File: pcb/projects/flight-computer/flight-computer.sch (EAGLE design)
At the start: 83 parts, among them IC1 ADG609RU, IC3 ADG609RU, P1 53048-0810, P2 53048-0810, U1 MCP73831/OT, U12 MAX31856MUD+, U13 MAX31856MUD+, U2 LP2985IM5-1.8/NOPB, U3 COM-13909, U4 ADXL377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

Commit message: add activation redundancy processor
- partial update of documentation to reflect this addition
- extra diagram of redundant activation
- pcb update to include a 32 pin qfn samd21 cortex m0 processor and necessary connections to bootload and flash over USB
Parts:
- removed ISM_SW: (no value), adafruit:PINHD-1X3CB
- added C7: 1uF, microbuilder:CAP_CERAMIC0603_NO
- added CN1: 4U#20329, microbuilder:USB_MICRO_20329_V2
- added IC2: ATSAMD21E, microbuilder:ATSAMD21E
- added JP1: (no value), pinhead:PINHD-1X4
- added JP2: (no value), pinhead:PINHD-1X2
- added R17: 470, rcl:R-US_R0603
- added SJ1: (no value), jumper:SJ
- added U10: SN74LVC1G08DCKR, SN74LVC1G08DCKR:SN74LVC1G08DCKR
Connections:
- removed net RADIO_OFF_SIG: ISM_SW.1, R18.1, U$1.33/A14
- new net !RESET: IC2./RESET, JP1.3
- new net D+: CN1.D+, IC2.PA25/I13/SERCOM3+5.3/D+
- new net D-: CN1.D-, IC2.PA24/I12/SERCOM3+5.2/D-
- new net PRI_ACT: SJ1.1, U$1.23/A9, U10.A
- new net SEC_ACT: IC2.PA00/EINT0/SERCOM1.0, SJ1.2, U10.B
- new net SEC_CS: IC2.PA08/I2C/AIN16/SERCOM0+2.0/I2SD1, U$1.27
- new net SEC_EN: IC2.PA01/EINT1/SERCOM1.1, R17.1, U$1.39/A20
- new net SWCLK: IC2.PA30/I10/SECOM1.2/SWCLK, JP1.2
- new net SWDIO: IC2.PA31/I11/SECOM1.3/SWDIO, JP1.1
- new net VBUS: CN1.VBUS
- new net VDDCORE1: C7.1, IC2.VDDCORE
- net 3V3: now also IC2.VDDA, IC2.VDDIN, JP2.1, U10.VCC; no longer ISM_SW.2
- net 3V3_RADIO: now also JP2.2, R18.1, U$1.33/A14; no longer ISM_SW.3
- net ACT: now also U10.Y; no longer U$1.23/A9
- net CS@TC1: now also IC2.PA02/EINT2/AIN0/Y0/VOUT
- net CS@TC2: now also IC2.PA10/I10/AIN18/SERCOM0+2.2/I2SCK
- net GND: now also C7.2, CN1.GND, IC2.GND, IC2.GNDA, JP1.4, R17.2, U10.GND
- net MISO: now also IC2.PA09/I2C/I9/AIN17/SERCOM0+2.1/I2SMC
- net MOSI: now also IC2.PA06/EINT6/AIN6/SERCOM0.2
- net SCLK: now also IC2.PA07/I7/AIN7/SERCOM0.3/I2SD0
- net TC1_FAULT: now also IC2.PA14/I14/SERCOM2+4.2
- net TC2_FAULT: now also IC2.PA15/I15/SERCOM3+4.3
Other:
- note added: "Secondary TC Monitoring System"
- note added: "Thanks to the design files and hard work done by Adafruit for the Trinket M0"
- note added: "https://cdn-learn.adafruit.com/assets/assets/000/049/778/original/adafruit_products_Adafruit_Trinket_M0.png?1514756138 https://github.com/adafruit/Adafruit-Trinket-M0-PCB"

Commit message: updated documentation, BOM and pinmap for activation redundancy processor
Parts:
- added JP3: (no value), pinhead:PINHD-1X2
- added R19: 100, rcl:R-US_R0603
- R17: value 470 -> 10k
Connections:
- new net BUZZER: JP3.1, U$1.24
- new net N$2: JP3.2, R19.2
- net GND: now also R19.1
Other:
- note added: "Activation Redundancy Processor"
- note added: "Buzzer Header"
- note removed: "Secondary TC Monitoring System"
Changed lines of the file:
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@@
 <part name="U$5" library="microbuilder" deviceset="VBUS" device=""/>
 <part name="SJ1" library="jumper" library_urn="urn:adsk.eagle:library:252" deviceset="SJ" device="" package3d_urn="urn:adsk.eagle:package:15471/1"/>
-<part name="R17" library="rcl" library_urn="urn:adsk.eagle:library:334" deviceset="R-US_" device="R0603" package3d_urn="urn:adsk.eagle:package:23555/3" value="470"/>
+<part name="R17" library="rcl" library_urn="urn:adsk.eagle:library:334" deviceset="R-US_" device="R0603" package3d_urn="urn:adsk.eagle:package:23555/3" value="10k"/>
+<part name="JP3" library="pinhead" deviceset="PINHD-1X2" device="" package3d_urn="urn:adsk.eagle:package:22435/2"/>
+<part name="R19" library="rcl" library_urn="urn:adsk.eagle:library:334" deviceset="R-US_" device="R0603" package3d_urn="urn:adsk.eagle:package:23555/3" value="100"/>
 </parts>
 <sheets>
@@
 <wire x1="63.5" y1="27.94" x2="71.12" y2="27.94" width="0.1524" layer="91"/>
 <label x="63.5" y="27.94" size="1.778" layer="95"/>
+</segment>
+</net>
+<net name="BUZZER" class="0">
+<segment>
+<pinref part="U$1" gate="G$1" pin="24"/>
+<wire x1="22.86" y1="33.02" x2="17.78" y2="33.02" width="0.1524" layer="91"/>
+<label x="10.16" y="33.02" size="1.778" layer="95"/>
 </segment>
 </net>
@@
 <sheet>
 <plain>
-<wire x1="147.32" y1="35.56" x2="147.32" y2="96.52" width="0.254" layer="94" style="longdash"/>
+<wire x1="147.32" y1="35.56" x2="147.32" y2="45.72" width="0.254" layer="94" style="longdash"/>
+<wire x1="147.32" y1="45.72" x2="147.32" y2="96.52" width="0.254" layer="94" style="longdash"/>
 <wire x1="147.32" y1="96.52" x2="147.32" y2="175.26" width="0.254" layer="94" style="longdash"/>
 <wire x1="147.32" y1="175.26" x2="147.32" y2="185.42" width="0.254" layer="94" style="longdash"/>
@@
 <wire x1="147.32" y1="96.52" x2="0" y2="96.52" width="0.254" layer="94" style="longdash"/>
 <text x="38.1" y="88.9" size="5.08" layer="94">Capacitive Sense Header</text>
+<wire x1="147.32" y1="45.72" x2="0" y2="45.72" width="0.254" layer="94" style="longdash"/>
+<text x="38.1" y="38.1" size="5.08" layer="94">Buzzer Header</text>
 </plain>
 <instances>
@@
 <instance part="GND6" gate="1" x="35.56" y="55.88" smashed="yes">
 <attribute name="VALUE" x="33.02" y="53.34" size="1.778" layer="96"/>
+</instance>
+<instance part="JP3" gate="G$1" x="66.04" y="22.86" smashed="yes">
+<attribute name="NAME" x="59.69" y="28.575" size="1.778" layer="95"/>
+<attribute name="VALUE" x="59.69" y="17.78" size="1.778" layer="96"/>
+</instance>
+<instance part="R19" gate="G$1" x="48.26" y="22.86" smashed="yes">
+<attribute name="NAME" x="44.45" y="24.3586" size="1.778" layer="95"/>
+<attribute name="VALUE" x="44.45" y="19.558" size="1.778" layer="96"/>
 </instance>
 </instances>
@@
 <wire x1="104.14" y1="157.48" x2="104.14" y2="109.22" width="0.1524" layer="91"/>
 </segment>
+<segment>
+<pinref part="R19" gate="G$1" pin="1"/>
+<wire x1="43.18" y1="22.86" x2="35.56" y2="22.86" width="0.1524" layer="91"/>
+<wire x1="35.56" y1="22.86" x2="35.56" y2="15.24" width="0.1524" layer="91"/>
+<label x="35.56" y="15.24" size="1.778" layer="95"/>
+</segment>
 </net>
 <net name="MISO" class="0">
@@
 </segment>
 </net>
+<net name="N$2" class="0">
+<segment>
+<pinref part="JP3" gate="G$1" pin="2"/>
+<pinref part="R19" gate="G$1" pin="2"/>
+<wire x1="63.5" y1="22.86" x2="53.34" y2="22.86" width="0.1524" layer="91"/>
+</segment>
+</net>
+<net name="BUZZER" class="0">
+<segment>
+<pinref part="JP3" gate="G$1" pin="1"/>
+<wire x1="63.5" y1="25.4" x2="35.56" y2="25.4" width="0.1524" layer="91"/>
+<label x="35.56" y="25.4" size="1.778" layer="95"/>
+</segment>
+</net>
 </nets>
 </sheet>
 <sheet>
 <plain>
-<text x="30.48" y="195.58" size="10.16" layer="94">Secondary TC Monitoring System</text>
+<text x="30.48" y="195.58" size="7.62" layer="94">Activation Redundancy Processor</text>
 <text x="119.38" y="149.86" size="2.032" layer="94">Thanks to the design files and hard work done by Adafruit for the Trinket M0</text>
 <text x="119.38" y="137.16" size="2.032" layer="94">https://cdn-learn.adafruit.com/assets/assets/000/049/778/original/adafruit_products_Adafruit_Trinket_M0.png?1514756138

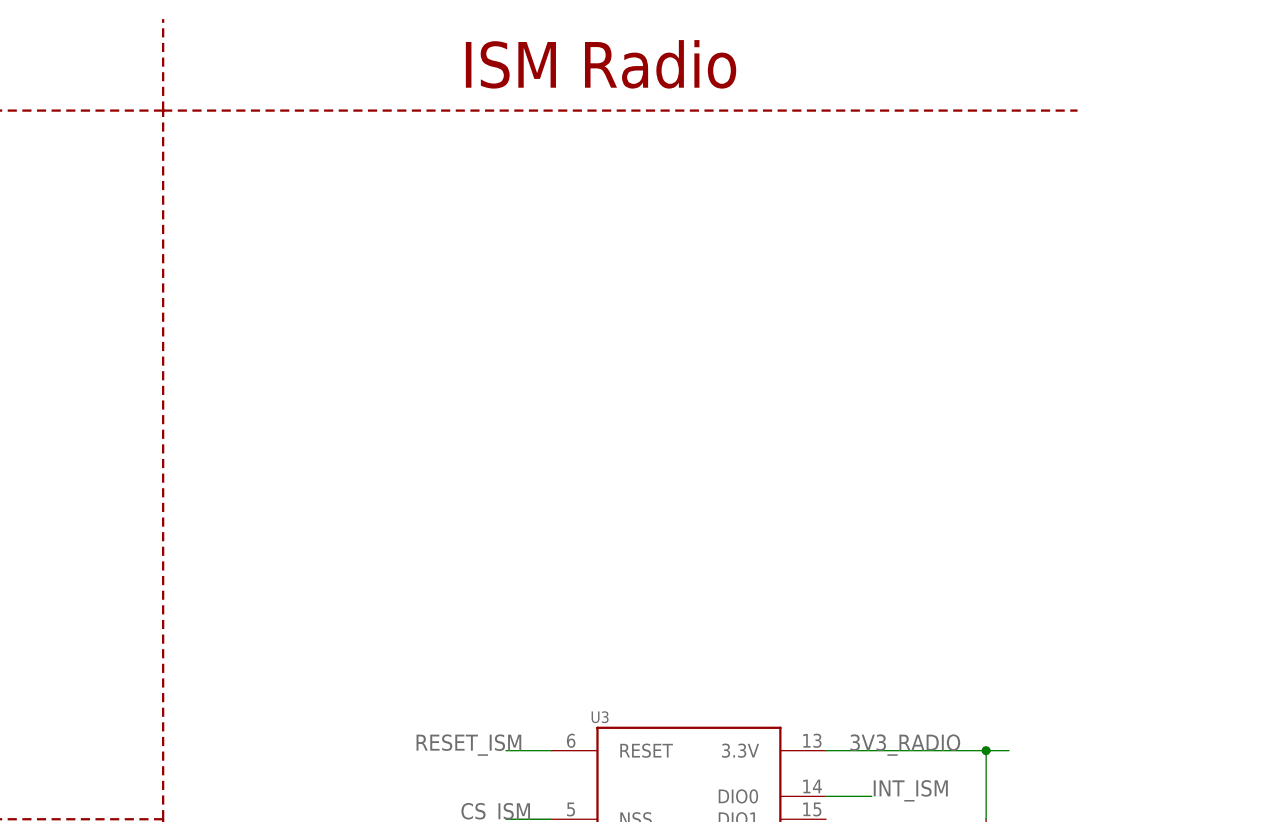
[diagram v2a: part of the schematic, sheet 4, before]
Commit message: add v1.1 pcb and documentation - added DSP310 barometric pressure sensor - add buzzer - add capacitive sense header - add more interface pins to the safety processor - add arduino pinouts for safety processor and refs on board silk - update flight computer hardware manual - add gerbers for v1.1 boards
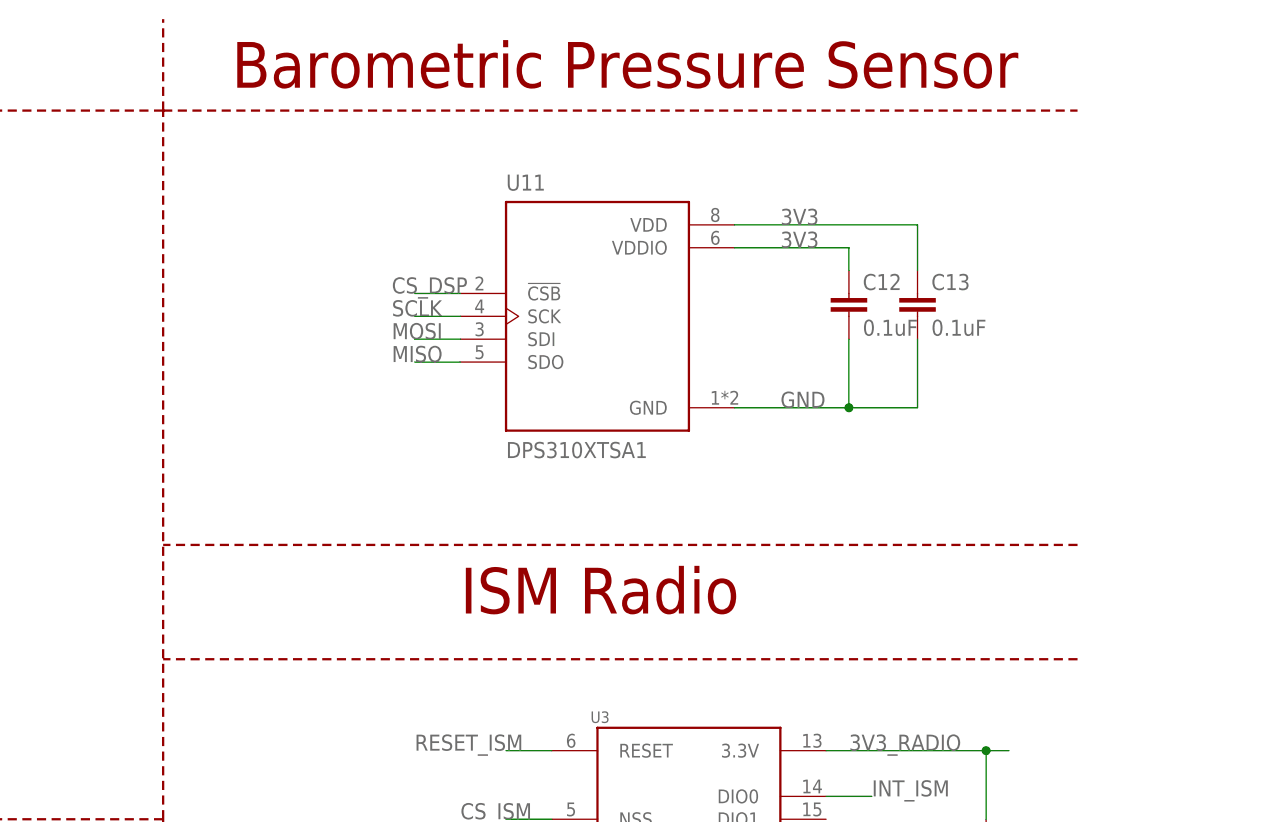
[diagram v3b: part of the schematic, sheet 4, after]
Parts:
- added C12, C13: 0.1uF, rcl:C-EUC0603
- added U11: DPS310XTSA1, DPS310XTSA1:DPS310XTSA1
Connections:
- net SEC_CS renamed SEC_CTRL_2
- net SEC_EN renamed SEC_CTRL_1
- new net CS_DSP: U$1.8, U11.!CSB
- net 3V3: now also C12.1, C13.1, U11.VDD, U11.VDDIO
- net GND: now also C12.2, C13.2, U11.GND
- net MISO: now also U11.SDO
- net MOSI: now also U11.SDI
- net MUX0: now also IC2.PA17/I2C/I1/SERCOM1+3.1
- net MUX1: now also IC2.PA18/I2/SERCOM1+3.2
- net SCLK: now also U11.SCK
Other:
- note added: "Barometric Pressure Sensor"
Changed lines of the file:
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@@
 <part name="JP3" library="pinhead" deviceset="PINHD-1X2" device="" package3d_urn="urn:adsk.eagle:package:22435/2"/>
 <part name="R19" library="rcl" library_urn="urn:adsk.eagle:library:334" deviceset="R-US_" device="R0603" package3d_urn="urn:adsk.eagle:package:23555/3" value="100"/>
+<part name="U11" library="DPS310XTSA1" deviceset="DPS310XTSA1" device=""/>
+<part name="C12" library="rcl" library_urn="urn:adsk.eagle:library:334" deviceset="C-EU" device="C0603" package3d_urn="urn:adsk.eagle:package:23616/2" value="0.1uF"/>
+<part name="C13" library="rcl" library_urn="urn:adsk.eagle:library:334" deviceset="C-EU" device="C0603" package3d_urn="urn:adsk.eagle:package:23616/2" value="0.1uF"/>
 </parts>
 <sheets>
@@
 </segment>
 </net>
-<net name="SEC_CS" class="0">
+<net name="SEC_CTRL_2" class="0">
 <segment>
 <pinref part="U$1" gate="G$1" pin="27"/>
@@
 </segment>
 </net>
-<net name="SEC_EN" class="0">
+<net name="SEC_CTRL_1" class="0">
 <segment>
 <pinref part="U$1" gate="G$1" pin="39/A20"/>
@@
 <wire x1="22.86" y1="33.02" x2="17.78" y2="33.02" width="0.1524" layer="91"/>
 <label x="10.16" y="33.02" size="1.778" layer="95"/>
+</segment>
+</net>
+<net name="CS_DSP" class="0">
+<segment>
+<pinref part="U$1" gate="G$1" pin="8"/>
+<wire x1="22.86" y1="48.26" x2="15.24" y2="48.26" width="0.1524" layer="91"/>
+<label x="15.24" y="48.26" size="1.778" layer="95"/>
 </segment>
 </net>
@@
 <wire x1="147.32" y1="175.26" x2="147.32" y2="185.42" width="0.254" layer="94" style="longdash"/>
 <wire x1="147.32" y1="175.26" x2="248.92" y2="175.26" width="0.254" layer="94" style="longdash"/>
-<text x="180.34" y="177.8" size="5.08" layer="94">ISM Radio</text>
+<text x="180.34" y="119.38" size="5.08" layer="94">ISM Radio</text>
 <text x="162.56" y="17.78" size="2.54" layer="94">KRUPS Main Board</text>
 <text x="238.76" y="7.62" size="2.54" layer="94">6.0</text>
@@
 <wire x1="147.32" y1="45.72" x2="0" y2="45.72" width="0.254" layer="94" style="longdash"/>
 <text x="38.1" y="38.1" size="5.08" layer="94">Buzzer Header</text>
+<wire x1="248.92" y1="127" x2="147.32" y2="127" width="0.254" layer="94" style="longdash"/>
+<wire x1="248.92" y1="114.3" x2="147.32" y2="114.3" width="0.254" layer="94" style="longdash"/>
+<text x="154.94" y="177.8" size="5.08" layer="94">Barometric Pressure Sensor</text>
 </plain>
 <instances>
@@
 <attribute name="NAME" x="44.45" y="24.3586" size="1.778" layer="95"/>
 <attribute name="VALUE" x="44.45" y="19.558" size="1.778" layer="96"/>
+</instance>
+<instance part="U11" gate="G$1" x="195.58" y="152.4" smashed="yes">
+<attribute name="NAME" x="185.42" y="166.37" size="1.778" layer="95"/>
+<attribute name="VALUE" x="185.42" y="138.43" size="1.778" layer="96" align="top-left"/>
+</instance>
+<instance part="C12" gate="G$1" x="223.52" y="154.94" smashed="yes">
+<attribute name="NAME" x="225.044" y="155.321" size="1.778" layer="95"/>
+<attribute name="VALUE" x="225.044" y="150.241" size="1.778" layer="96"/>
+</instance>
+<instance part="C13" gate="G$1" x="231.14" y="154.94" smashed="yes">
+<attribute name="NAME" x="232.664" y="155.321" size="1.778" layer="95"/>
+<attribute name="VALUE" x="232.664" y="150.241" size="1.778" layer="96"/>
 </instance>
 </instances>
@@
 <label x="35.56" y="15.24" size="1.778" layer="95"/>
 </segment>
+<segment>
+<pinref part="U11" gate="G$1" pin="GND"/>
+<label x="215.9" y="142.24" size="1.778" layer="95"/>
+<pinref part="C13" gate="G$1" pin="2"/>
+<wire x1="231.14" y1="149.86" x2="231.14" y2="142.24" width="0.1524" layer="91"/>
+<wire x1="231.14" y1="142.24" x2="223.52" y2="142.24" width="0.1524" layer="91"/>
+<pinref part="C12" gate="G$1" pin="2"/>
+<wire x1="223.52" y1="142.24" x2="210.82" y2="142.24" width="0.1524" layer="91"/>
+<wire x1="223.52" y1="149.86" x2="223.52" y2="142.24" width="0.1524" layer="91"/>
+<junction x="223.52" y="142.24"/>
+</segment>
 </net>
 <net name="MISO" class="0">
@@
 <label x="182.88" y="88.9" size="1.778" layer="95"/>
 </segment>
+<segment>
+<pinref part="U11" gate="G$1" pin="SDO"/>
+<wire x1="180.34" y1="147.32" x2="175.26" y2="147.32" width="0.1524" layer="91"/>
+<label x="172.72" y="147.32" size="1.778" layer="95"/>
+</segment>
 </net>
 <net name="MOSI" class="0">
@@
 <label x="182.88" y="91.44" size="1.778" layer="95"/>
 </segment>
+<segment>
+<pinref part="U11" gate="G$1" pin="SDI"/>
+<wire x1="180.34" y1="149.86" x2="175.26" y2="149.86" width="0.1524" layer="91"/>
+<label x="172.72" y="149.86" size="1.778" layer="95"/>
+</segment>
 </net>
 <net name="SCLK" class="0">
@@
 <wire x1="190.5" y1="93.98" x2="185.42" y2="93.98" width="0.1524" layer="91"/>
 <label x="182.88" y="93.98" size="1.778" layer="95"/>
+</segment>
+<segment>
+<pinref part="U11" gate="G$1" pin="SCK"/>
+<wire x1="180.34" y1="152.4" x2="175.26" y2="152.4" width="0.1524" layer="91"/>
+<label x="172.72" y="152.4" size="1.778" layer="95"/>
 </segment>
 </net>
@@
 <wire x1="63.5" y1="25.4" x2="35.56" y2="25.4" width="0.1524" layer="91"/>
 <label x="35.56" y="25.4" size="1.778" layer="95"/>
+</segment>
+</net>
+<net name="3V3" class="0">
+<segment>
+<pinref part="U11" gate="G$1" pin="VDD"/>
+<label x="215.9" y="162.56" size="1.778" layer="95"/>
+<wire x1="210.82" y1="162.56" x2="231.14" y2="162.56" width="0.1524" layer="91"/>
+<pinref part="C13" gate="G$1" pin="1"/>
+<wire x1="231.14" y1="162.56" x2="231.14" y2="157.48" width="0.1524" layer="91"/>
+</segment>
+<segment>
+<pinref part="U11" gate="G$1" pin="VDDIO"/>
+<label x="215.9" y="160.02" size="1.778" layer="95"/>
+<pinref part="C12" gate="G$1" pin="1"/>
+<wire x1="223.52" y1="157.48" x2="223.52" y2="160.02" width="0.1524" layer="91"/>
+<wire x1="223.52" y1="160.02" x2="210.82" y2="160.02" width="0.1524" layer="91"/>
+</segment>
+</net>
+<net name="CS_DSP" class="0">
+<segment>
+<pinref part="U11" gate="G$1" pin="!CSB"/>
+<wire x1="180.34" y1="154.94" x2="175.26" y2="154.94" width="0.1524" layer="91"/>
+<label x="172.72" y="154.94" size="1.778" layer="95"/>
 </segment>
 </net>
@@
 </segment>
 </net>
-<net name="SEC_EN" class="0">
-<segment>
-<pinref part="IC2" gate="G$1" pin="PA01/EINT1/SERCOM1.1"/>
-<label x="124.46" y="127" size="1.778" layer="95"/>
-<pinref part="R17" gate="G$1" pin="1"/>
-<wire x1="114.3" y1="127" x2="142.24" y2="127" width="0.1524" layer="91"/>
-</segment>
-</net>
 <net name="CS@TC1" class="0">
 <segment>
@@
 <wire x1="114.3" y1="111.76" x2="124.46" y2="111.76" width="0.1524" layer="91"/>
 <label x="124.46" y="111.76" size="1.778" layer="95"/>
-</segment>
-</net>
-<net name="SEC_CS" class="0">
-<segment>
-<pinref part="IC2" gate="G$1" pin="PA08/I2C/AIN16/SERCOM0+2.0/I2SD1"/>
-<wire x1="114.3" y1="106.68" x2="124.46" y2="106.68" width="0.1524" layer="91"/>
-<label x="124.46" y="106.68" size="1.778" layer="95"/>
 </segment>
 </net>
@@
 </segment>
 </net>
+<net name="MUX0" class="0">
+<segment>
+<pinref part="IC2" gate="G$1" pin="PA17/I2C/I1/SERCOM1+3.1"/>
+<wire x1="114.3" y1="81.28" x2="121.92" y2="81.28" width="0.1524" layer="91"/>
+<label x="121.92" y="81.28" size="1.778" layer="95"/>
+</segment>
+</net>
+<net name="MUX1" class="0">
+<segment>
+<pinref part="IC2" gate="G$1" pin="PA18/I2/SERCOM1+3.2"/>
+<wire x1="114.3" y1="78.74" x2="121.92" y2="78.74" width="0.1524" layer="91"/>
+<label x="121.92" y="78.74" size="1.778" layer="95"/>
+</segment>
+</net>
+<net name="SEC_CTRL_1" class="0">
+<segment>
+<pinref part="IC2" gate="G$1" pin="PA01/EINT1/SERCOM1.1"/>
+<label x="124.46" y="127" size="1.778" layer="95"/>
+<pinref part="R17" gate="G$1" pin="1"/>
+<wire x1="114.3" y1="127" x2="142.24" y2="127" width="0.1524" layer="91"/>
+</segment>
+</net>
+<net name="SEC_CTRL_2" class="0">
+<segment>
+<pinref part="IC2" gate="G$1" pin="PA08/I2C/AIN16/SERCOM0+2.0/I2SD1"/>
+<wire x1="114.3" y1="106.68" x2="124.46" y2="106.68" width="0.1524" layer="91"/>
+<label x="124.46" y="106.68" size="1.778" layer="95"/>
+</segment>
+</net>
